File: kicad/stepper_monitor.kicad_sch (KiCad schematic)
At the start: 53 parts, among them J1 Conn_01x04_Male, J2 Conn_01x04_Male, J3 Conn_01x02_Male, J4 USB_C_Receptacle_USB2.0, J5 JTAG, M1 Motor-simple_stepper_motor_an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, Q1 UMH3N, Q2 PJA3439, SW1 SW_Push, U1 CP2102N-A01-GQFN28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

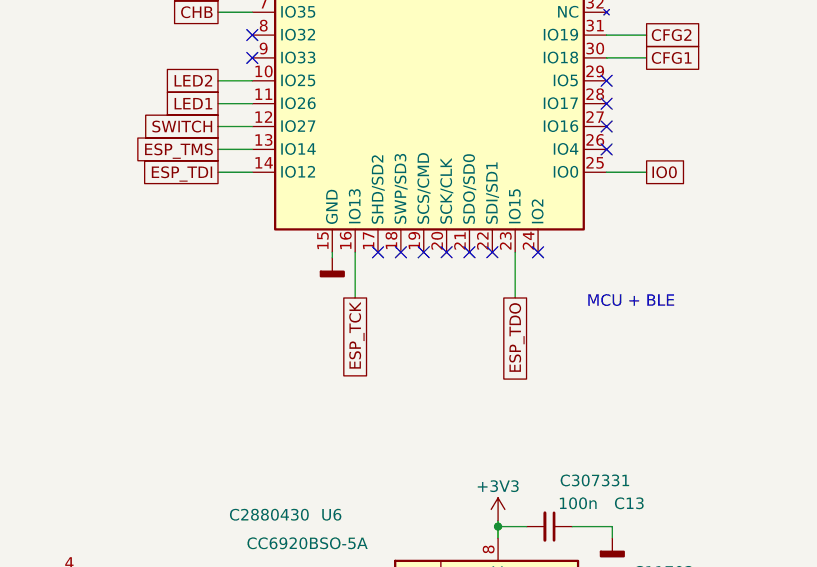
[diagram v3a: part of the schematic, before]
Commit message: Added test point.
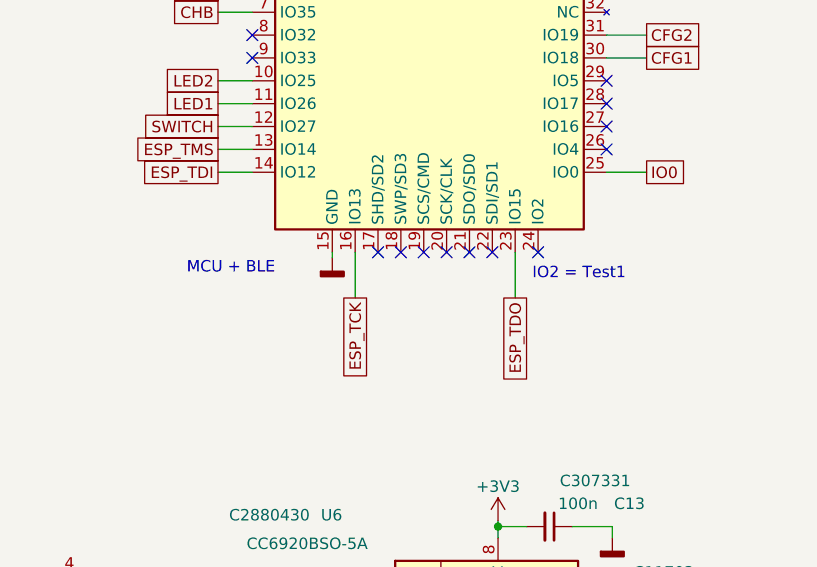
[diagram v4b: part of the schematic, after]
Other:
- note added: "IO2 = Test1"
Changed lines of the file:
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@@
   (no_connect (at 116.205 77.47))
   (no_connect (at 46.99 118.11))
-  (no_connect (at 251.46 75.565))
   (no_connect (at 46.99 115.57))
   (no_connect (at 116.205 118.11))
+  (no_connect (at 251.46 75.565))
   (no_connect (at 116.205 87.63))
   (no_connect (at 116.205 120.65))
@@
     (effects (font (size 1.27 1.27)) (justify right bottom))
   )
+  (text "IO2 = Test1" (at 250.825 78.74 0)
+    (effects (font (size 1.27 1.27)) (justify left bottom))
+  )
   (text "Configuration" (at 162.56 142.875 180)
     (effects (font (size 1.27 1.27)) (justify right bottom))
@@
     (effects (font (size 1.27 1.27)) (justify right bottom))
   )
-  (text "MCU + BLE" (at 266.7 81.915 180)
+  (text "MCU + BLE" (at 222.25 78.105 180)
     (effects (font (size 1.27 1.27)) (justify right bottom))
   )

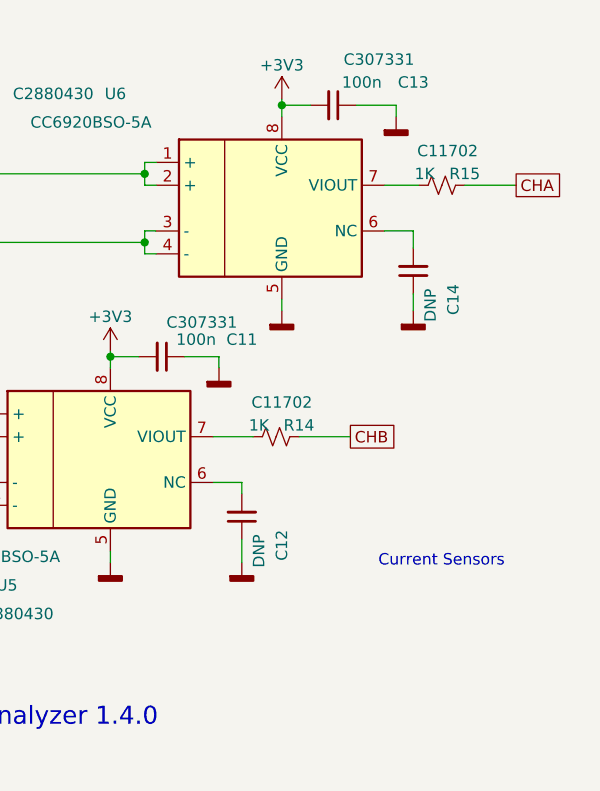
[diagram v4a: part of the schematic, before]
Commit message: Added ADC capacitors.
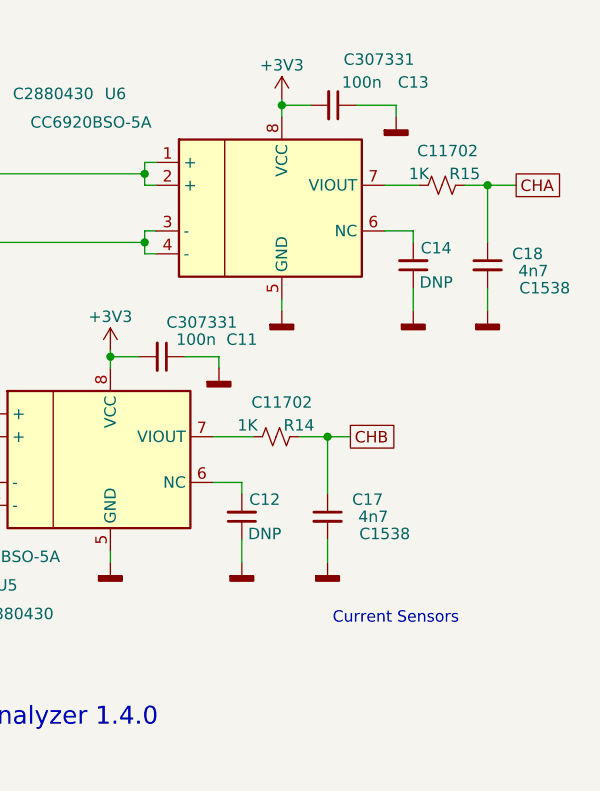
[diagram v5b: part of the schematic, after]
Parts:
- added C17, C18: 4n7, Capacitor_SMD:C_0402_1005Metric, symbol Device:C_Small
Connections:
- net CHA: now also C18.1
- net CHB: now also C17.1
- net GNDD: now also C17.2, C18.2
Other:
- moved on the sheet: C14
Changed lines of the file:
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@@
   (junction (at 93.98 51.435) (diameter 0) (color 0 0 0 0)
   )
+  (junction (at 269.875 114.935) (diameter 0) (color 0 0 0 0)
+  )
   (junction (at 113.03 161.29) (diameter 0) (color 0 0 0 0)
   )
@@
   )
   (junction (at 82.55 51.435) (diameter 0) (color 0 0 0 0)
+  )
+  (junction (at 252.095 142.875) (diameter 0) (color 0 0 0 0)
   )
   (junction (at 67.31 37.465) (diameter 0) (color 0 0 0 0)
@@
     (stroke (width 0) (type default) (color 0 0 0 0))
   )
+  (wire (pts (xy 269.875 114.935) (xy 273.05 114.935))
+    (stroke (width 0) (type default) (color 0 0 0 0))
+  )
   (wire (pts (xy 259.08 43.815) (xy 263.525 43.815))
     (stroke (width 0) (type default) (color 0 0 0 0))
@@
     (stroke (width 0) (type default) (color 0 0 0 0))
   )
+  (wire (pts (xy 248.92 142.875) (xy 252.095 142.875))
+    (stroke (width 0) (type default) (color 0 0 0 0))
+  )
   (wire (pts (xy 144.145 37.465) (xy 147.955 37.465))
     (stroke (width 0) (type default) (color 0 0 0 0))
@@
     (stroke (width 0) (type default) (color 0 0 0 0))
   )
-  (wire (pts (xy 248.92 142.875) (xy 254.635 142.875))
-    (stroke (width 0) (type default) (color 0 0 0 0))
-  )
-  (wire (pts (xy 267.335 114.935) (xy 273.05 114.935))
-    (stroke (width 0) (type default) (color 0 0 0 0))
-  )
   (wire (pts (xy 93.98 47.625) (xy 93.98 51.435))
     (stroke (width 0) (type default) (color 0 0 0 0))
@@
     (stroke (width 0) (type default) (color 0 0 0 0))
   )
+  (wire (pts (xy 252.095 142.875) (xy 254.635 142.875))
+    (stroke (width 0) (type default) (color 0 0 0 0))
+  )
   (wire (pts (xy 53.975 43.815) (xy 53.975 45.085))
     (stroke (width 0) (type default) (color 0 0 0 0))
@@
     (stroke (width 0) (type default) (color 0 0 0 0))
   )
+  (wire (pts (xy 269.875 114.935) (xy 269.875 121.285))
+    (stroke (width 0) (type default) (color 0 0 0 0))
+  )
   (wire (pts (xy 231.775 121.285) (xy 231.775 122.555))
     (stroke (width 0) (type default) (color 0 0 0 0))
@@
     (stroke (width 0) (type default) (color 0 0 0 0))
   )
+  (wire (pts (xy 252.095 154.305) (xy 252.095 156.845))
+    (stroke (width 0) (type default) (color 0 0 0 0))
+  )
   (wire (pts (xy 247.015 106.045) (xy 247.015 107.315))
     (stroke (width 0) (type default) (color 0 0 0 0))
@@
     (stroke (width 0) (type default) (color 0 0 0 0))
   )
-  (wire (pts (xy 261.62 120.015) (xy 261.62 121.92))
+  (wire (pts (xy 267.335 114.935) (xy 269.875 114.935))
+    (stroke (width 0) (type default) (color 0 0 0 0))
+  )
+  (wire (pts (xy 261.62 120.015) (xy 261.62 121.285))
     (stroke (width 0) (type default) (color 0 0 0 0))
   )
@@
     (stroke (width 0) (type default) (color 0 0 0 0))
   )
+  (wire (pts (xy 252.095 142.875) (xy 252.095 149.225))
+    (stroke (width 0) (type default) (color 0 0 0 0))
+  )
   (wire (pts (xy 111.125 69.85) (xy 113.03 69.85))
     (stroke (width 0) (type default) (color 0 0 0 0))
   )
+  (wire (pts (xy 269.875 126.365) (xy 269.875 128.905))
+    (stroke (width 0) (type default) (color 0 0 0 0))
+  )
   (wire (pts (xy 69.85 35.56) (xy 69.85 37.465))
     (stroke (width 0) (type default) (color 0 0 0 0))
@@
     (stroke (width 0) (type default) (color 0 0 0 0))
   )
-  (wire (pts (xy 261.62 127) (xy 261.62 128.905))
+  (wire (pts (xy 261.62 126.365) (xy 261.62 128.905))
     (stroke (width 0) (type default) (color 0 0 0 0))
   )
@@
     (stroke (width 0) (type default) (color 0 0 0 0))
   )
-  (text "Current Sensors" (at 271.78 157.48 180)
+  (text "Current Sensors" (at 266.7 163.83 180)
     (effects (font (size 1.27 1.27)) (justify right bottom))
   )
@@
     (pin "1")
   )
+  (symbol (lib_id "power:GNDD") (at 252.095 156.845 0) (unit 1)
+    (in_bom yes) (on_board yes)
+    (property "Reference" "#PWR018" (id 0) (at 252.095 163.195 0)
+      (effects (font (size 1.27 1.27)) hide)
+    )
+    (property "Value" "GNDD" (id 1) (at 252.1966 160.782 0)
+      (effects (font (size 1.27 1.27)) hide)
+    )
+    (property "Footprint" "" (id 2) (at 252.095 156.845 0)
+      (effects (font (size 1.27 1.27)) hide)
+    )
+    (property "Datasheet" "" (id 3) (at 252.095 156.845 0)
+      (effects (font (size 1.27 1.27)) hide)
+    )
+    (pin "1")
+  )
   (symbol (lib_id "Device:C_Small") (at 101.6 45.085 180) (unit 1)
     (in_bom yes) (on_board yes)
@@
     (pin "2")
   )
+  (symbol (lib_id "Device:C_Small") (at 269.875 123.825 0) (unit 1)
+    (in_bom yes) (on_board yes)
+    (property "Reference" "C18" (id 0) (at 274.32 122.555 0))
+    (property "Value" "4n7" (id 1) (at 274.955 124.46 0))
+    (property "Footprint" "Capacitor_SMD:C_0402_1005Metric" (id 2) (at 269.875 123.825 0)
+      (effects (font (size 1.27 1.27)) hide)
+    )
+    (property "Datasheet" "~" (id 3) (at 269.875 123.825 0)
+      (effects (font (size 1.27 1.27)) hide)
+    )
+    (property "LCSC" "C1538" (id 4) (at 276.225 126.365 0))
+    (pin "1")
+    (pin "2")
+  )
   (symbol (lib_id "Regulator_Linear:AMS1117-3.3") (at 118.11 37.465 0) (unit 1)
     (in_bom yes) (on_board yes)
@@
     (in_bom yes) (on_board yes)
     (property "Reference" "R15" (id 0) (at 267.335 113.665 90))
-    (property "Value" "1K" (id 1) (at 262.89 113.665 90))
+    (property "Value" "1K" (id 1) (at 262.255 113.665 90))
     (property "Footprint" "Resistor_SMD:R_0402_1005Metric" (id 2) (at 264.795 114.935 0)
       (effects (font (size 1.27 1.27)) hide)
@@
   (symbol (lib_id "Device:C_Small") (at 242.57 151.765 180) (unit 1)
     (in_bom yes) (on_board yes)
-    (property "Reference" "C12" (id 0) (at 247.015 154.94 90))
-    (property "Value" "DNP" (id 1) (at 244.475 155.575 90))
+    (property "Reference" "C12" (id 0) (at 245.11 149.86 0))
+    (property "Value" "DNP" (id 1) (at 245.11 153.67 0))
     (property "Footprint" "Capacitor_SMD:C_0402_1005Metric" (id 2) (at 242.57 151.765 0)
       (effects (font (size 1.27 1.27)) hide)
@@
     (pin "1")
     (pin "2")
+  )
+  (symbol (lib_id "power:GNDD") (at 269.875 128.905 0) (unit 1)
+    (in_bom yes) (on_board yes)
+    (property "Reference" "#PWR019" (id 0) (at 269.875 135.255 0)
+      (effects (font (size 1.27 1.27)) hide)
+    )
+    (property "Value" "GNDD" (id 1) (at 269.9766 132.842 0)
+      (effects (font (size 1.27 1.27)) hide)
+    )
+    (property "Footprint" "" (id 2) (at 269.875 128.905 0)
+      (effects (font (size 1.27 1.27)) hide)
+    )
+    (property "Datasheet" "" (id 3) (at 269.875 128.905 0)
+      (effects (font (size 1.27 1.27)) hide)
+    )
+    (pin "1")
   )
   (symbol (lib_id "Device:C_Small") (at 252.73 106.045 270) (unit 1)
@@
     (pin "2")
   )
-  (symbol (lib_id "Device:C_Small") (at 261.62 124.46 180) (unit 1)
-    (in_bom yes) (on_board yes)
-    (property "Reference" "C14" (id 0) (at 266.065 127.635 90))
-    (property "Value" "DNP" (id 1) (at 263.525 128.27 90))
-    (property "Footprint" "Capacitor_SMD:C_0402_1005Metric" (id 2) (at 261.62 124.46 0)
-      (effects (font (size 1.27 1.27)) hide)
-    )
-    (property "Datasheet" "~" (id 3) (at 261.62 124.46 0)
+  (symbol (lib_id "Device:C_Small") (at 261.62 123.825 180) (unit 1)
+    (in_bom yes) (on_board yes)
+    (property "Reference" "C14" (id 0) (at 264.16 121.92 0))
+    (property "Value" "DNP" (id 1) (at 264.16 125.73 0))
+    (property "Footprint" "Capacitor_SMD:C_0402_1005Metric" (id 2) (at 261.62 123.825 0)
+      (effects (font (size 1.27 1.27)) hide)
+    )
+    (property "Datasheet" "~" (id 3) (at 261.62 123.825 0)
       (effects (font (size 1.27 1.27)) hide)
     )
@@
     )
     (pin "1")
+  )
+  (symbol (lib_id "Device:C_Small") (at 252.095 151.765 0) (unit 1)
+    (in_bom yes) (on_board yes)
+    (property "Reference" "C17" (id 0) (at 256.54 149.86 0))
+    (property "Value" "4n7" (id 1) (at 257.175 151.765 0))
+    (property "Footprint" "Capacitor_SMD:C_0402_1005Metric" (id 2) (at 252.095 151.765 0)
+      (effects (font (size 1.27 1.27)) hide)
+    )
+    (property "Datasheet" "~" (id 3) (at 252.095 151.765 0)
+      (effects (font (size 1.27 1.27)) hide)
+    )
+    (property "LCSC" "C1538" (id 4) (at 258.445 153.67 0))
+    (pin "1")
+    (pin "2")
   )
   (symbol (lib_id "Switch:SW_Push") (at 67.31 175.895 90) (unit 1)
@@
     (in_bom yes) (on_board yes)
     (property "Reference" "R14" (id 0) (at 248.92 141.605 90))
-    (property "Value" "1K" (id 1) (at 244.475 141.605 90))
+    (property "Value" "1K" (id 1) (at 243.205 141.605 90))
     (property "Footprint" "Resistor_SMD:R_0402_1005Metric" (id 2) (at 246.38 142.875 0)
       (effects (font (size 1.27 1.27)) hide)
@@
       (reference "#PWR017") (unit 1) (value "GNDD") (footprint "")
     )
+    (path "/073be000-12b6-4f57-b721-4ec95d0e58fb"
+      (reference "#PWR018") (unit 1) (value "GNDD") (footprint "")
+    )
+    (path "/33f931c5-360c-483b-8ce4-ac978337d60f"
+      (reference "#PWR019") (unit 1) (value "GNDD") (footprint "")
+    )
     (path "/5d3263f0-2044-4033-8250-d44c87ba32dc"
       (reference "#PWR0101") (unit 1) (value "GNDD") (footprint "")
@@
       (reference "C16") (unit 1) (value "10u") (footprint "Capacitor_SMD:C_0603_1608Metric")
     )
+    (path "/b4307130-80c7-4433-8dd4-c0c8baa37eb9"
+      (reference "C17") (unit 1) (value "4n7") (footprint "Capacitor_SMD:C_0402_1005Metric")
+    )
+    (path "/16636ebd-e2e9-4c4c-a031-868c68e0891b"
+      (reference "C18") (unit 1) (value "4n7") (footprint "Capacitor_SMD:C_0402_1005Metric")
+    )
     (path "/00000000-0000-0000-0000-00006319144c"

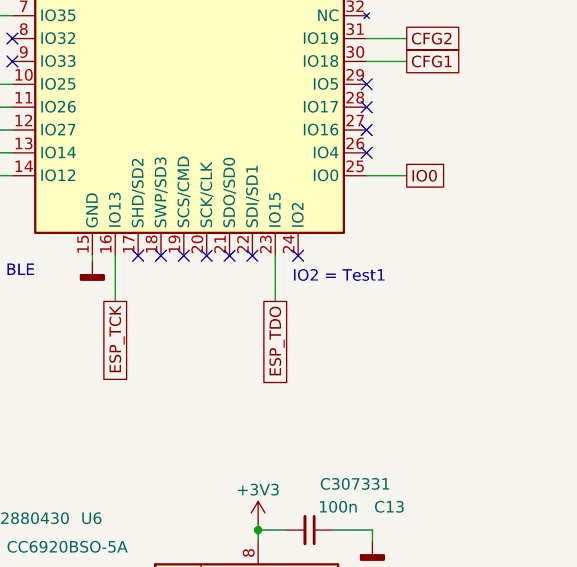
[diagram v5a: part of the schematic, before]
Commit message: Added pin TEST2.
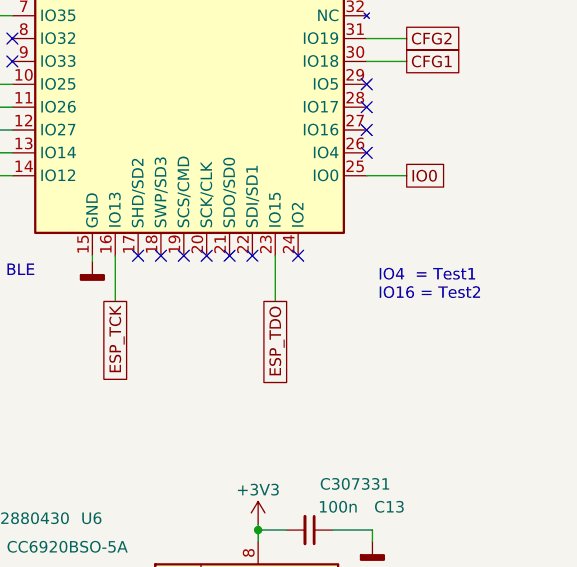
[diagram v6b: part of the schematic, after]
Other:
- note added: "IO4 = Test1 IO16 = Test2"
- note removed: "IO2 = Test1"
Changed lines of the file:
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@@
     (effects (font (size 1.27 1.27)) (justify right bottom))
   )
-  (text "IO2 = Test1" (at 250.825 78.74 0)
+  (text "IO4  = Test1\nIO16 = Test2" (at 260.35 80.645 0)
     (effects (font (size 1.27 1.27)) (justify left bottom))
   )

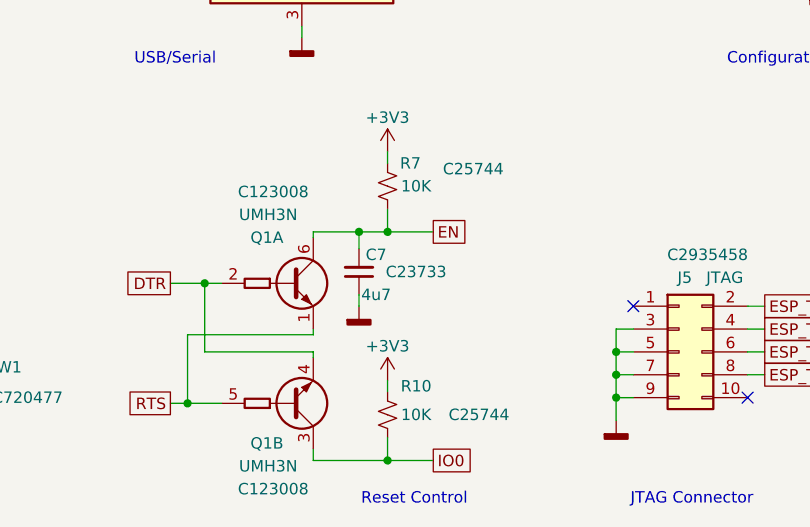
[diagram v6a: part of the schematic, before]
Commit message: Updated capacitor value from 4u7 to 2u2.
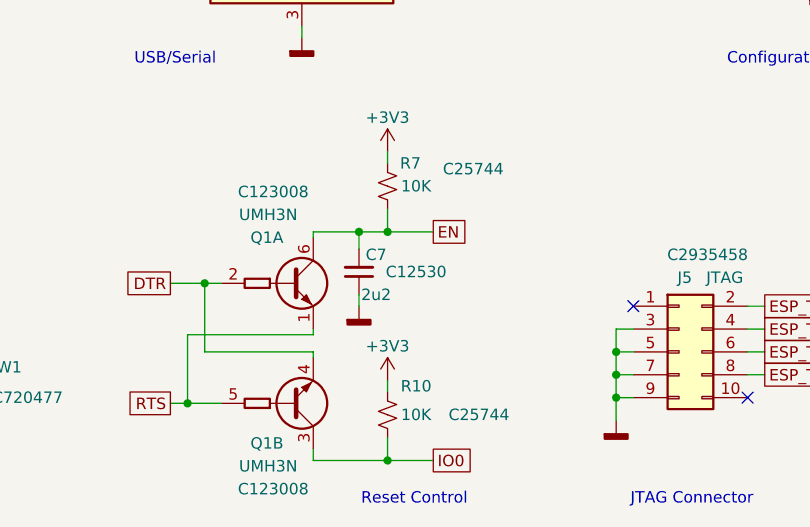
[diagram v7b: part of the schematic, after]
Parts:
- C7: value 4u7 -> 2u2; LCSC C23733 -> C12530
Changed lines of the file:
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@@
     (in_bom yes) (on_board yes)
     (property "Reference" "C7" (id 0) (at 111.76 163.83 0))
-    (property "Value" "4u7" (id 1) (at 111.76 168.275 0))
+    (property "Value" "2u2" (id 1) (at 111.76 168.275 0))
     (property "Footprint" "Capacitor_SMD:C_0402_1005Metric" (id 2) (at 109.855 165.735 0)
       (effects (font (size 1.27 1.27)) hide)
@@
       (effects (font (size 1.27 1.27)) hide)
     )
-    (property "LCSC" "C23733" (id 4) (at 116.205 165.735 0))
+    (property "LCSC" "C12530" (id 4) (at 116.205 165.735 0))
     (pin "1")
     (pin "2")
@@
     )
     (path "/a9a9c830-a019-40b4-bcda-03bad99cf4b0"
-      (reference "C7") (unit 1) (value "4u7") (footprint "Capacitor_SMD:C_0402_1005Metric")
+      (reference "C7") (unit 1) (value "2u2") (footprint "Capacitor_SMD:C_0402_1005Metric")
     )
     (path "/1d49663a-f566-4513-a796-a3c1bbd0d1b0"

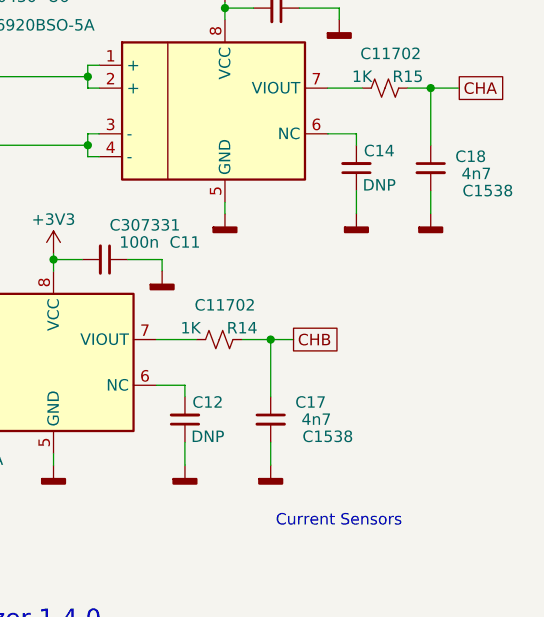
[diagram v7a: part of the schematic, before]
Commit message: Change adc filter caps from 4.7n to 2.2n
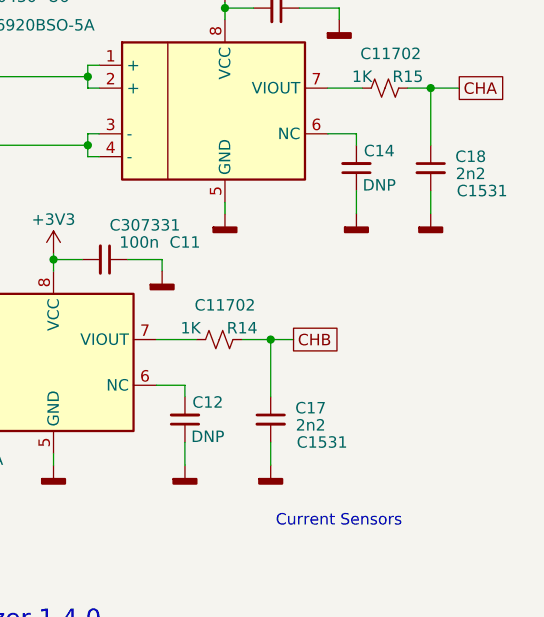
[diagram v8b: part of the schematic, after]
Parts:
- C17, C18: value 4n7 -> 2n2; LCSC C1538 -> C1531
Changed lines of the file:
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@@
     (in_bom yes) (on_board yes)
     (property "Reference" "C18" (id 0) (at 274.32 122.555 0))
-    (property "Value" "4n7" (id 1) (at 274.955 124.46 0))
+    (property "Value" "2n2" (id 1) (at 274.32 124.46 0))
     (property "Footprint" "Capacitor_SMD:C_0402_1005Metric" (id 2) (at 269.875 123.825 0)
       (effects (font (size 1.27 1.27)) hide)
@@
       (effects (font (size 1.27 1.27)) hide)
     )
-    (property "LCSC" "C1538" (id 4) (at 276.225 126.365 0))
+    (property "LCSC" "C1531" (id 4) (at 275.59 126.365 0))
     (pin "1")
     (pin "2")
@@
   (symbol (lib_id "Device:C_Small") (at 252.095 151.765 0) (unit 1)
     (in_bom yes) (on_board yes)
-    (property "Reference" "C17" (id 0) (at 256.54 149.86 0))
-    (property "Value" "4n7" (id 1) (at 257.175 151.765 0))
+    (property "Reference" "C17" (id 0) (at 256.54 150.495 0))
+    (property "Value" "2n2" (id 1) (at 256.54 152.4 0))
     (property "Footprint" "Capacitor_SMD:C_0402_1005Metric" (id 2) (at 252.095 151.765 0)
       (effects (font (size 1.27 1.27)) hide)
@@
       (effects (font (size 1.27 1.27)) hide)
     )
-    (property "LCSC" "C1538" (id 4) (at 258.445 153.67 0))
+    (property "LCSC" "C1531" (id 4) (at 257.81 154.305 0))
     (pin "1")
     (pin "2")
@@
     )
     (path "/b4307130-80c7-4433-8dd4-c0c8baa37eb9"
-      (reference "C17") (unit 1) (value "4n7") (footprint "Capacitor_SMD:C_0402_1005Metric")
+      (reference "C17") (unit 1) (value "2n2") (footprint "Capacitor_SMD:C_0402_1005Metric")
     )
     (path "/16636ebd-e2e9-4c4c-a031-868c68e0891b"
-      (reference "C18") (unit 1) (value "4n7") (footprint "Capacitor_SMD:C_0402_1005Metric")
+      (reference "C18") (unit 1) (value "2n2") (footprint "Capacitor_SMD:C_0402_1005Metric")
     )
     (path "/00000000-0000-0000-0000-00006319144c"
